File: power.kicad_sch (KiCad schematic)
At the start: 14 parts, among them U5 LTC3111EDE

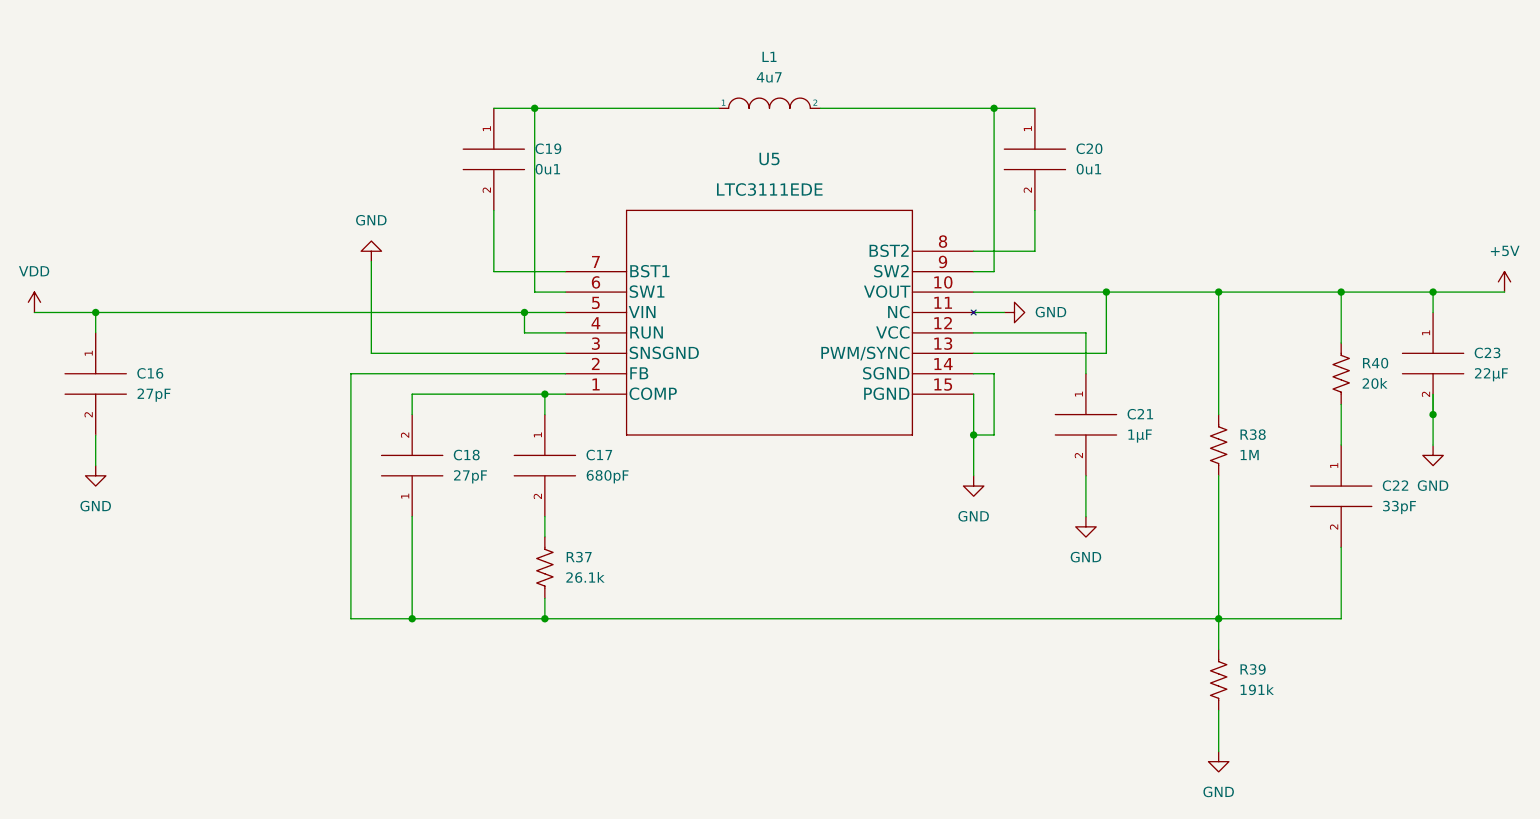
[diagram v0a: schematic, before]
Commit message: First week after winter break. Changed Power circuit design to use different DC to DC converter Setting correct footprints for the components like resistors and capacitors.
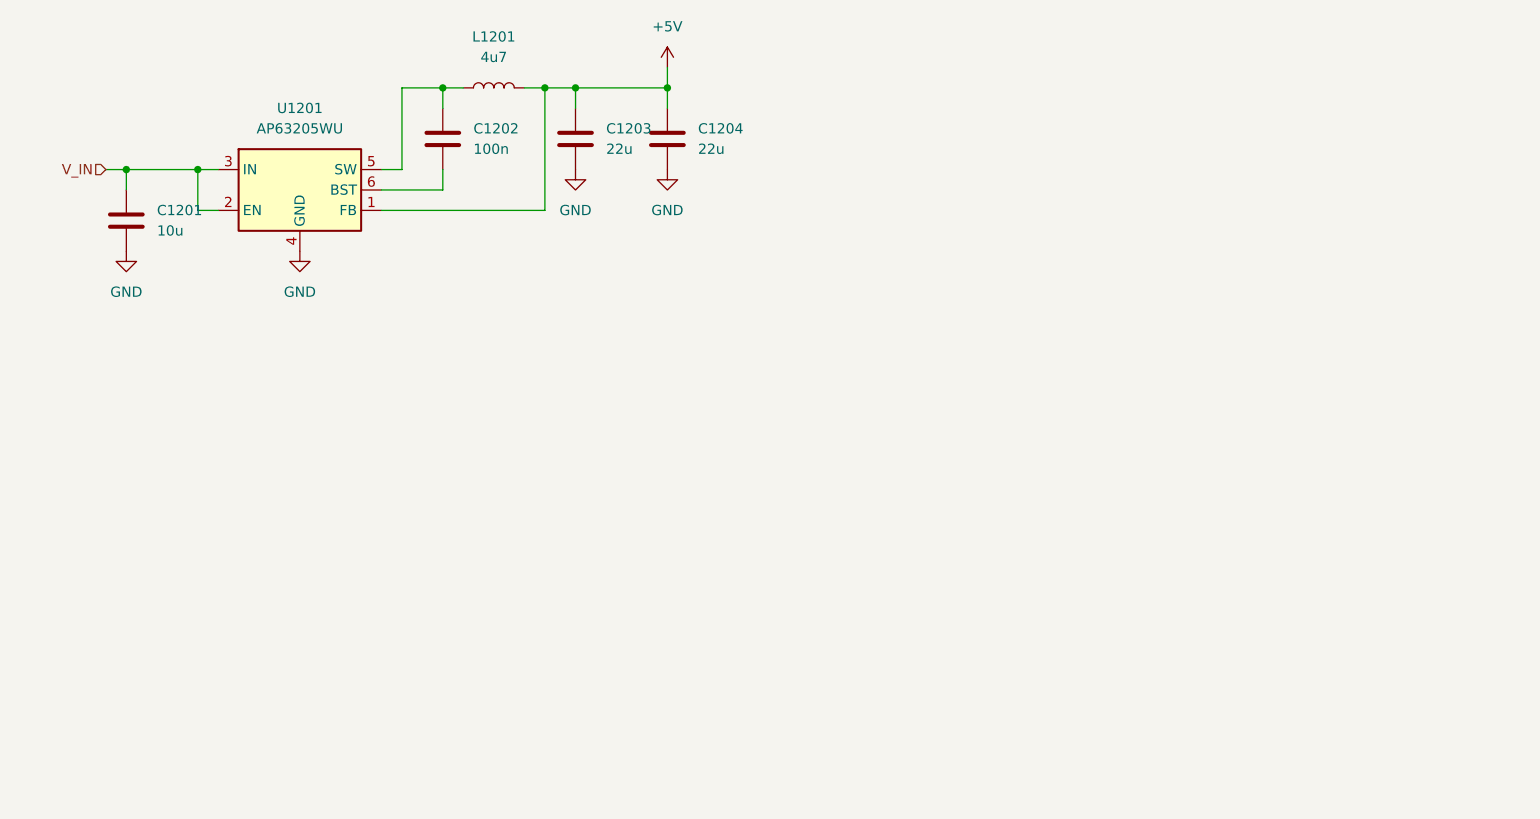
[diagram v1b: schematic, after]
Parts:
- removed C16, C18: 27pF, Capacitor_SMD:C_0201_0603Metric, symbol pspice:C
- removed C17: 680pF, Capacitor_SMD:C_0603_1608Metric, symbol pspice:C
- removed C19, C20: 0u1, Capacitor_SMD:C_0201_0603Metric, symbol pspice:C
- removed C21: 1µF, Capacitor_SMD:C_0201_0603Metric, symbol pspice:C
- removed C22: 33pF, Capacitor_SMD:C_0603_1608Metric, symbol pspice:C
- removed C23: 22µF, Capacitor_SMD:C_1206_3216Metric, symbol pspice:C
- removed L1: 4u7, Inductor_SMD:L_6.3x6.3_H3, symbol pspice:INDUCTOR
- removed R37: 26.1k, Resistor_SMD:R_0201_0603Metric, symbol Device:R_US
- removed R38: 1M, Resistor_SMD:R_0201_0603Metric, symbol Device:R_US
- removed R39: 191k, Resistor_SMD:R_0201_0603Metric, symbol Device:R_US
- removed R40: 20k, Resistor_SMD:R_0201_0603Metric, symbol Device:R_US
- removed U5: LTC3111EDE, Custom:LTC3111EDE-TRPBF, symbol BuckBoost1:LTC3111EDE-PBF
- added C1201: 10u, Capacitor_SMD:C_0603_1608Metric, symbol Device:C
- added C1202: 100n, Capacitor_SMD:C_0805_2012Metric, symbol Device:C
- added C1203, C1204: 22u, Capacitor_SMD:C_0603_1608Metric, symbol Device:C
- added L1201: 4u7, symbol Device:L
- added U1201: AP63205WU, Package_TO_SOT_SMD:TSOT-23-6, symbol Regulator_Switching:AP63205WU
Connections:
- net +5V: now also C1203.1, C1204.1, L1201.2, U1201.1 (FB)
- net GND: now also C1201.2, C1203.2, C1204.2, U1201.4 (GND)
- new net: C1202.1, L1201.1, U1201.5 (SW)
- new net: C1202.2, U1201.6 (BST)
- new net V_IN: C1201.1, U1201.2 (EN), U1201.3 (IN)

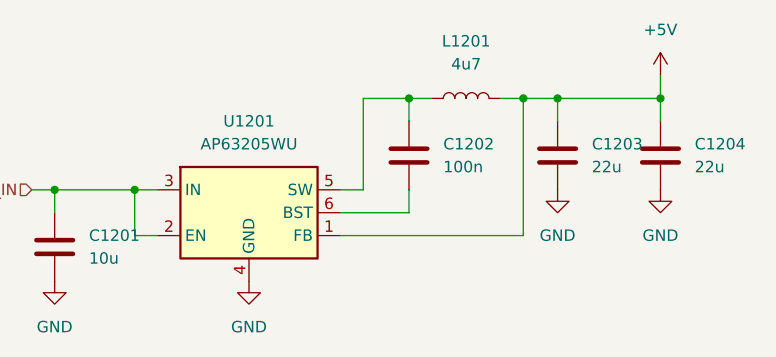
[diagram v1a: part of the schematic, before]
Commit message: Weekend progress
Things that remain:
4 LEDs to Microcontroller
7-Seg to Microcontroller
LCD to Microcontroller
Microphone and Speakers to Microcontroller
Power circuitry
USB-C connector
Reset and Boot buttons
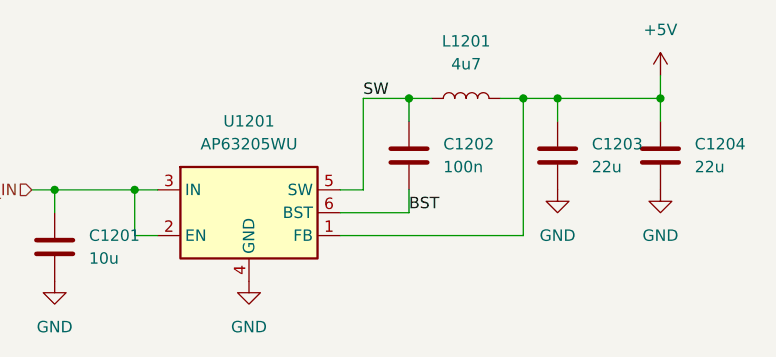
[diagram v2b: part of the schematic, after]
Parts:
- L1201: footprint (none) -> Inductor_SMD:L_1008_2520Metric; Manufacturer_Name (none) -> Samsung Electro-Mechanics; Manufacturer_Part_Number (none) -> CIGW252010GL4R7MNE
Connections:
- net SW: now reaches C1202.1, L1201.1, U1201.5 (SW)
- net BST: now reaches C1202.2, U1201.6 (BST)
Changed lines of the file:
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@@
     (stroke (width 0) (type default) (color 0 0 0 0))
+  )
+  (label "SW" (at 102.87 52.07 0)
+    (effects (font (size 1.27 1.27)) (justify left bottom))
+  )
+  (label "BST" (at 107.95 64.77 0)
+    (effects (font (size 1.27 1.27)) (justify left bottom))
   )
   (hierarchical_label "V_IN" (shape input) (at 66.04 62.23 180)
@@
     (property "Reference" "L1201" (id 0) (at 114.3 45.72 90))
     (property "Value" "4u7" (id 1) (at 114.3 48.26 90))
-    (property "Footprint" "" (id 2) (at 114.3 52.07 0)
+    (property "Footprint" "Inductor_SMD:L_1008_2520Metric" (id 2) (at 114.3 52.07 0)
       (effects (font (size 1.27 1.27)) hide)
     )
@@
       (effects (font (size 1.27 1.27)) hide)
     )
+    (property "Manufacturer_Name" "Samsung Electro-Mechanics" (id 4) (at 114.3 52.07 0)
+      (effects (font (size 1.27 1.27)) hide)
+    )
+    (property "Manufacturer_Part_Number" "CIGW252010GL4R7MNE" (id 5) (at 114.3 52.07 0)
+      (effects (font (size 1.27 1.27)) hide)
+    )

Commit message: Update BOM and POC files
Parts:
- U1201: Manufacturer_Name (none) -> Diodes Incorporated; Manufacturer_Part_Number (none) -> AP63205WU-7
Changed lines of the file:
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@@
+      (effects (font (size 1.27 1.27)) hide)
+    )
+    (property "Manufacturer_Name" "Diodes Incorporated" (id 4) (at 90.17 64.77 0)
+      (effects (font (size 1.27 1.27)) hide)
+    )
+    (property "Manufacturer_Part_Number" "AP63205WU-7" (id 5) (at 90.17 64.77 0)
       (effects (font (size 1.27 1.27)) hide)
     )
